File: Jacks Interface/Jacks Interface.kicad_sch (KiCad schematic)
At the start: 11 parts, among them J1 INPUT, J10 EARTH, J11 RETURN, J2 To board GND, J3 To board IN, J4 From battery minus, J5 To board OUT, J6 OUTPUT, J7 SEND, J8 To board SEND, J9 To board RETURN

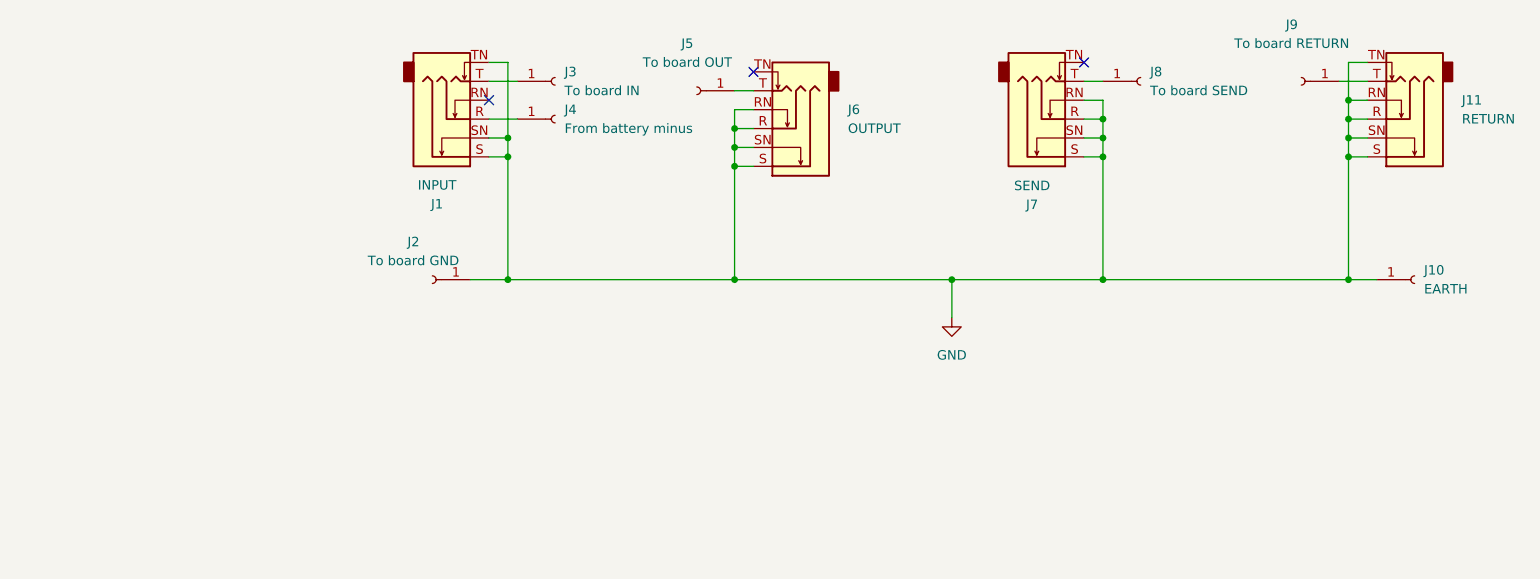
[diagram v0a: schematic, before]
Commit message: fix: 回路の修正
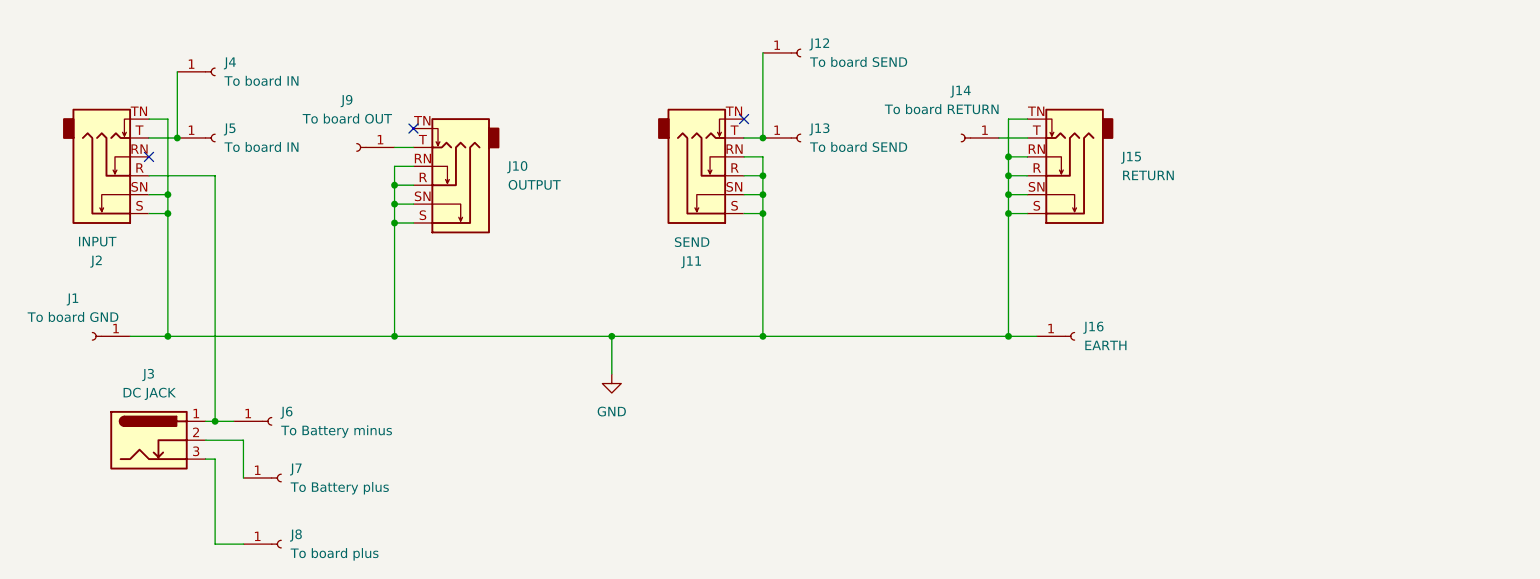
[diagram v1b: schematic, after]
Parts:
- added J12: To board SEND, My_Parts:Header_Pin_1p_Large, symbol Connector:Conn_01x01_Female
- added J3: DC JACK, symbol Connector:Barrel_Jack_Switch_Pin3Ring
- added J6: To Battery minus, symbol Connector:Conn_01x01_Female
- added J7: To Battery plus, symbol Connector:Conn_01x01_Female
- added J8: To board plus, symbol Connector:Conn_01x01_Female
- J14: renamed from J9; value To board RETURN -> To board RETURN
- J4: value From battery minus -> To board IN
- renumbered J2 to J1, J6 to J10, J7 to J11, J8 to J13, J11 to J15, J10 to J16, J1 to J2, J3 to J5, J5 to J9
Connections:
- net at J2.T, J5.1 (Pin_1): now also J4.1 (Pin_1)
- net at J2.R: now also J3.1, J6.1 (Pin_1); no longer J4.1 (Pin_1)
- net at J11.T, J13.1 (Pin_1): now also J12.1 (Pin_1)
- new net: J3.3, J8.1 (Pin_1)
- new net: J3.2, J7.1 (Pin_1)
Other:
- company: (none) -> ARAGI (https://101010.fun)
- title: (none) -> Jacks Interface
- moved on the sheet: J1, J10, J11, J13, J14, J15, J16, J2, J5, J9

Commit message: fix: jack interface修正
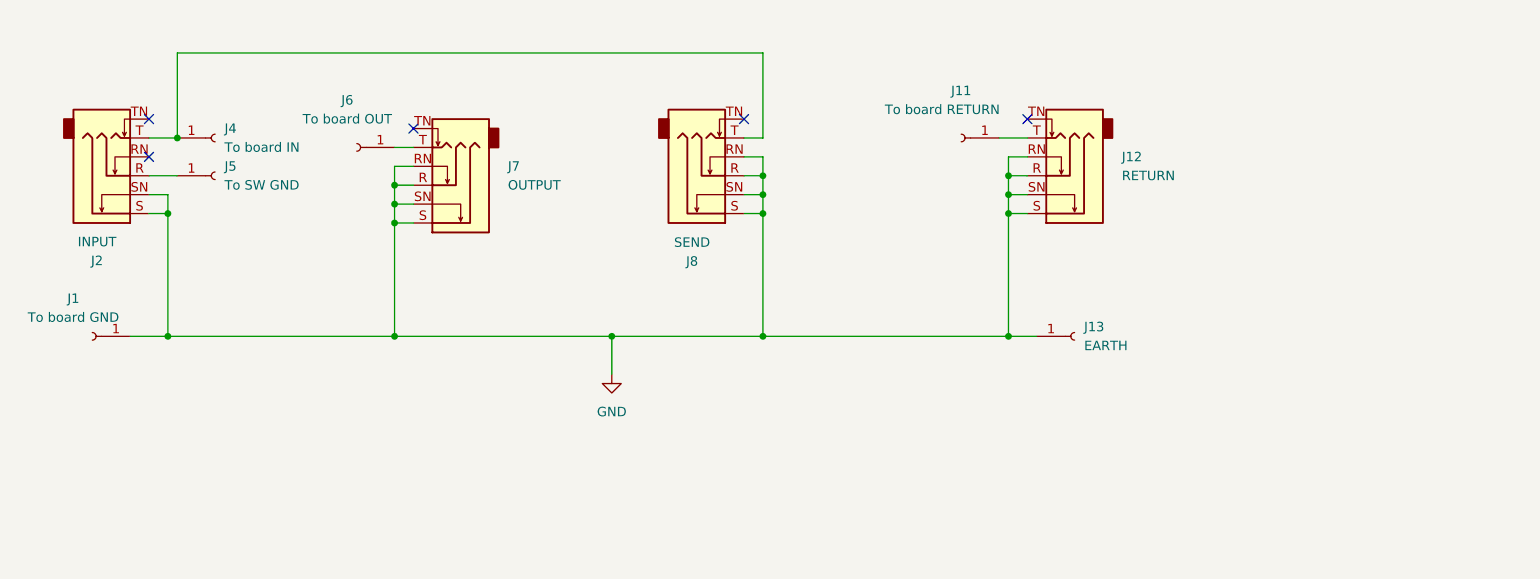
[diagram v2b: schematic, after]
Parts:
- removed J12, J13: To board SEND, My_Parts:Header_Pin_1p_Large, symbol Connector:Conn_01x01_Female
- removed J3: DC JACK, symbol Connector:Barrel_Jack_Switch_Pin3Ring
- removed J4: To board IN, My_Parts:Header_Pin_1p_Large, symbol Connector:Conn_01x01_Female
- removed J7: To Battery plus, symbol Connector:Conn_01x01_Female
- removed J8: To board plus, symbol Connector:Conn_01x01_Female
- J1: footprint My_Parts:Header_Pin_1p_Large -> My_Parts:Header_Pin_1p_Large_GND
- J13: renamed from J16; footprint My_Parts:Header_Pin_1p_Large -> My_Parts:Header_Pin_1p_Large_GND
- J4: renamed from J5; footprint My_Parts:Header_Pin_1p_Large -> My_Parts:Header_Pin_1p_Large_IN
- J5: renamed from J6; value To Battery minus -> To SW GND; footprint (none) -> My_Parts:Header_Pin_1p_Large_GND
- J6: renamed from J9; footprint My_Parts:Header_Pin_1p_Large -> My_Parts:Header_Pin_1p_Large_OUT
- renumbered J14 to J11, J15 to J12, J10 to J7, J11 to J8
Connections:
- net GND: no longer J12.TN, J2.TN
- net at J2.T, J4.1 (Pin_1): now also J8.T
- no-connect marks 3 -> 5
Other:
- moved on the sheet: J5
